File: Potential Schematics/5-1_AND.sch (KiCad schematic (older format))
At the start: 2 parts, among them U193 74LS09, U195 74LS09

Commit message: Adding Multiply Devide
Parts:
- U193, U195: symbol 74LS09 -> 4-bit_processor-rescue:74LS09
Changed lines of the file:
@@
-EESchema Schematic File Version 2
-LIBS:power
-LIBS:device
-LIBS:switches
-LIBS:relays
-LIBS:motors
-LIBS:transistors
-LIBS:conn
-LIBS:linear
-LIBS:regul
-LIBS:74xx
-LIBS:cmos4000
-LIBS:adc-dac
-LIBS:memory
-LIBS:xilinx
-LIBS:microcontrollers
-LIBS:dsp
-LIBS:microchip
-LIBS:analog_switches
-LIBS:motorola
-LIBS:texas
-LIBS:intel
-LIBS:audio
-LIBS:interface
-LIBS:digital-audio
-LIBS:philips
-LIBS:display
-LIBS:cypress
-LIBS:siliconi
-LIBS:opto
-LIBS:atmel
-LIBS:contrib
-LIBS:valves
+EESchema Schematic File Version 4
 LIBS:4-bit_processor-cache
-EELAYER 25 0
+EELAYER 26 0
 EELAYER END
 $Descr A4 11693 8268
 encoding utf-8
-Sheet 382 449
+Sheet 382 451
 Title "5:1 AND"
 Date "2018-09-14"
@@
 Q
 $Comp
-L 74LS09 U193
+L 4-bit_processor-rescue:74LS09 U193
 U 2 1 5BAF0199
 P 3100 2100
@@
 $EndComp
 $Comp
-L 74LS09 U193
+L 4-bit_processor-rescue:74LS09 U193
 U 3 1 5BAF025C
 P 3100 3100
@@
 $EndComp
 $Comp
-L 74LS09 U193
+L 4-bit_processor-rescue:74LS09 U193
 U 4 1 5BAF03A5
 P 4750 3050
@@
 $EndComp
 $Comp
-L 74LS09 U195
+L 4-bit_processor-rescue:74LS09 U195
 U 1 1 5BAF044F
 P 8000 3500

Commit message: Finished PCB
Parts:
- U207: renamed from U193; footprint (none) -> Daniel_Kopp:DIP-14_300_ELL
- U209: renamed from U195; footprint (none) -> Daniel_Kopp:DIP-14_300_ELL

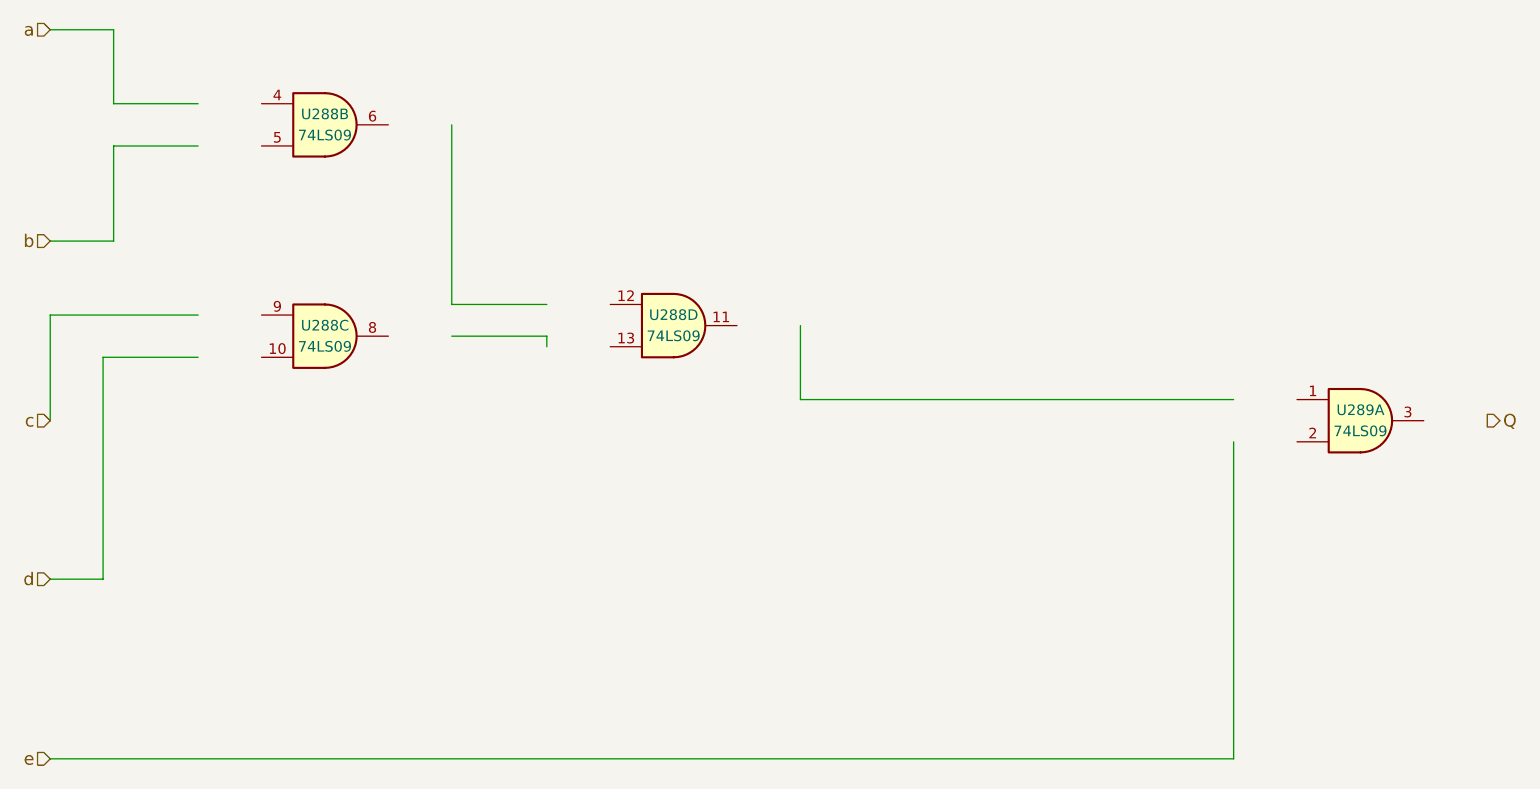
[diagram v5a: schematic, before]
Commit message: In the middle of adding ROM
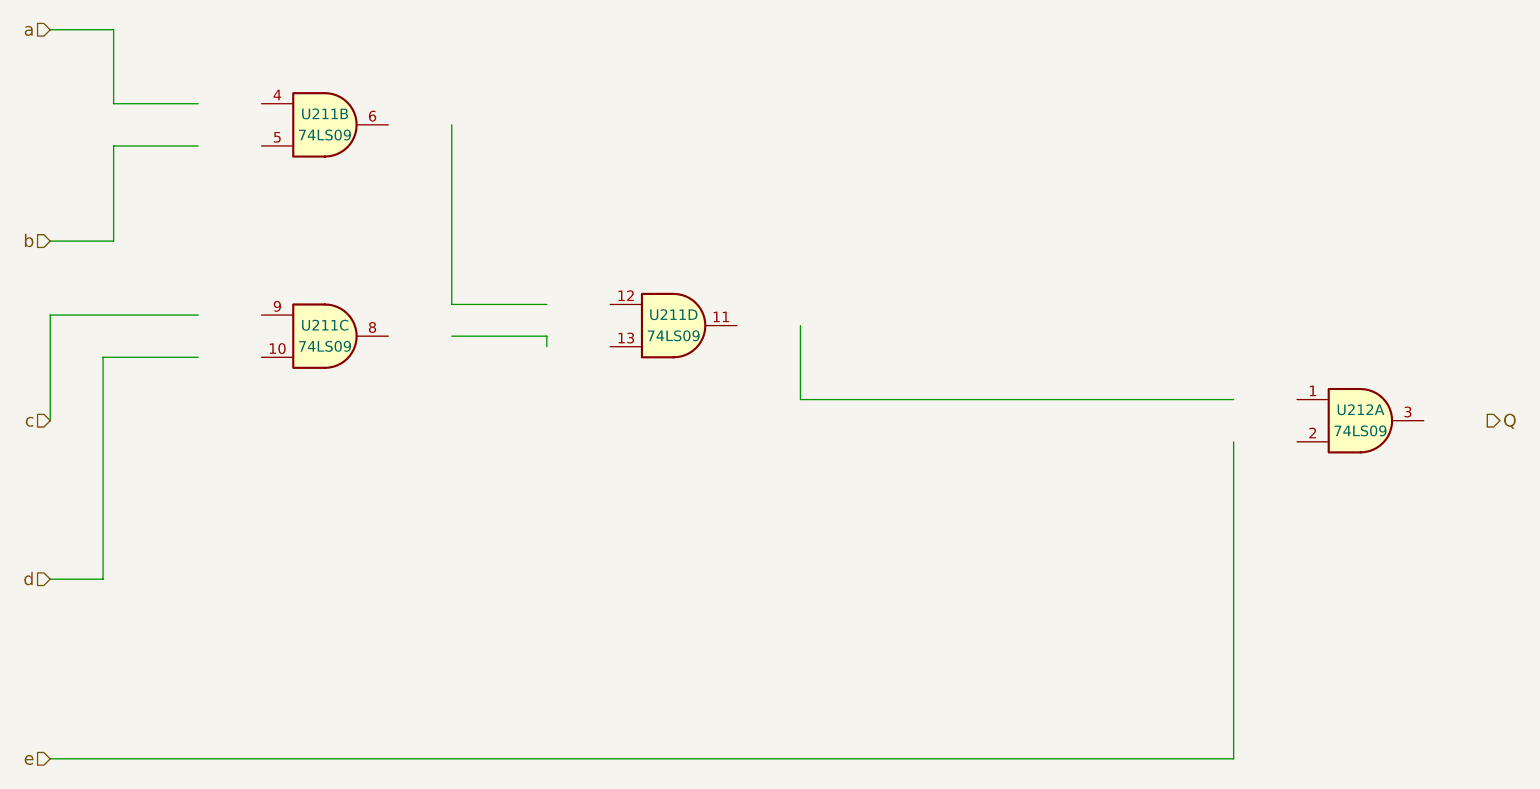
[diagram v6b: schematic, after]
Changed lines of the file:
@@
 $Descr A4 11693 8268
 encoding utf-8
-Sheet 382 902
+Sheet 382 1330
 Title "5:1 AND"
 Date "2018-09-14"
@@
 AR Path="/5B9D167A/5B9C0EA0/5BAE2F4B/5BC8F503/5BB23562/5BAF0199" Ref="U287"  Part="2"
 AR Path="/5B9D167A/5B9C0EA0/5BAE2F4B/5BC8F503/5BB2356A/5BAF0199" Ref="U288"  Part="2"
-F 0 "U288" H 3100 2150 50  0000 C CNN
+F 0 "U211" H 3100 2150 50  0000 C CNN
 F 1 "74LS09" H 3100 2050 50  0000 C CNN
 F 2 "Daniel_Kopp:DIP-14_300_ELL" H 3100 2100 50  0001 C CNN
@@
 AR Path="/5B9D167A/5B9C0EA0/5BAE2F4B/5BC8F503/5BB23562/5BAF025C" Ref="U287"  Part="3"
 AR Path="/5B9D167A/5B9C0EA0/5BAE2F4B/5BC8F503/5BB2356A/5BAF025C" Ref="U288"  Part="3"
-F 0 "U288" H 3100 3150 50  0000 C CNN
+F 0 "U211" H 3100 3150 50  0000 C CNN
 F 1 "74LS09" H 3100 3050 50  0000 C CNN
 F 2 "Daniel_Kopp:DIP-14_300_ELL" H 3100 3100 50  0001 C CNN
@@
 AR Path="/5B9D167A/5B9C0EA0/5BAE2F4B/5BC8F503/5BB23562/5BAF03A5" Ref="U287"  Part="4"
 AR Path="/5B9D167A/5B9C0EA0/5BAE2F4B/5BC8F503/5BB2356A/5BAF03A5" Ref="U288"  Part="4"
-F 0 "U288" H 4750 3100 50  0000 C CNN
+F 0 "U211" H 4750 3100 50  0000 C CNN
 F 1 "74LS09" H 4750 3000 50  0000 C CNN
 F 2 "Daniel_Kopp:DIP-14_300_ELL" H 4750 3050 50  0001 C CNN
@@
 AR Path="/5B9D167A/5B9C0EA0/5BAE2F4B/5BC8F503/5BB23562/5BAF044F" Ref="U288"  Part="1"
 AR Path="/5B9D167A/5B9C0EA0/5BAE2F4B/5BC8F503/5BB2356A/5BAF044F" Ref="U289"  Part="1"
-F 0 "U289" H 8000 3550 50  0000 C CNN
+F 0 "U212" H 8000 3550 50  0000 C CNN
 F 1 "74LS09" H 8000 3450 50  0000 C CNN
 F 2 "Daniel_Kopp:DIP-14_300_ELL" H 8000 3500 50  0001 C CNN
